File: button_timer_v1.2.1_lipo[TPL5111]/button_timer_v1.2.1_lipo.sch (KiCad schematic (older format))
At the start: 23 parts, among them J1 Conn_01x05_Female, SW1 SW_Push, SW2 SW_Push, U2 AP2112K-3.3, U3 TPL5111, X1 ESP-12E

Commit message: 3D Models etwas verbessert
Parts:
- C5: footprint handsolder:C_0805_2012handsodermod -> handsolder:C_0402_1005Metric_Pad0.74x0.62mm_HandSoldermod
- J1: footprint Connector_PinHeader_2.54mm:PinHeader_1x05_P2.54mm_Vertical -> Connector_PinSocket_2.54mm:PinSocket_1x05_P2.54mm_Vertical
- SW1: footprint Button_Switch_THT:SW_PUSH_6mm -> Button_Switch_THT:SW_PUSH_6mm_H8mm
- SW2: footprint Button_Switch_SMD:SW_SPST_EVQPE1 -> Button_Switch_SMD:SW_SPST_B3U-1000P
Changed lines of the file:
@@
 F 0 "SW2" H 8000 3385 50  0000 C CNN
 F 1 "SW_Push" H 8000 3294 50  0000 C CNN
-F 2 "Button_Switch_SMD:SW_SPST_EVQPE1" H 8000 3300 50  0001 C CNN
+F 2 "Button_Switch_SMD:SW_SPST_B3U-1000P" H 8000 3300 50  0001 C CNN
 F 3 "~" H 8000 3300 50  0001 C CNN
 	1    8000 3100
@@
 F 0 "SW1" H 1100 5935 50  0000 C CNN
 F 1 "SW_Push" H 1100 5844 50  0000 C CNN
-F 2 "Button_Switch_THT:SW_PUSH_6mm" H 1100 5850 50  0001 C CNN
+F 2 "Button_Switch_THT:SW_PUSH_6mm_H8mm" H 1100 5850 50  0001 C CNN
 F 3 "~" H 1100 5850 50  0001 C CNN
 	1    1100 5650
@@
 F 0 "J1" H 8128 3476 50  0000 L CNN
 F 1 "Conn_01x05_Female" H 8128 3385 50  0000 L CNN
-F 2 "Connector_PinHeader_2.54mm:PinHeader_1x05_P2.54mm_Vertical" H 8100 3450 50  0001 C CNN
+F 2 "Connector_PinSocket_2.54mm:PinSocket_1x05_P2.54mm_Vertical" H 8100 3450 50  0001 C CNN
 F 3 "~" H 8100 3450 50  0001 C CNN
 	1    8100 3450
@@
 F 0 "C5" V 2148 4850 50  0000 C CNN
 F 1 "100nF" V 2239 4850 50  0000 C CNN
-F 2 "handsolder:C_0805_2012handsodermod" H 2438 4700 50  0001 C CNN
+F 2 "handsolder:C_0402_1005Metric_Pad0.74x0.62mm_HandSoldermod" H 2438 4700 50  0001 C CNN
 F 3 "~" H 2400 4850 50  0001 C CNN
 	1    2400 4850

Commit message: cap between esp vcc and ground added
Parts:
- added C6: TAJB476M010TNJ, CAPPM3528X210N, symbol SamacSys_Parts:TAJB476M010TNJ
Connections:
- net GND: now also C6.2
- net VCC: now also C6.1
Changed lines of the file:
@@
 Text Label 2250 4850 2    50   ~ 0
 GND
+Text Label 5300 4200 0    50   ~ 0
+GND
+$Comp
+L SamacSys_Parts:TAJB476M010TNJ C6
+U 1 1 603708C9
+P 5300 3700
+F 0 "C6" V 5504 3830 50  0000 L CNN
+F 1 "TAJB476M010TNJ" V 5595 3830 50  0000 L CNN
+F 2 "CAPPM3528X210N" H 5650 3750 50  0001 L CNN
+F 3 "http://datasheets.avx.com/TAJ.pdf" H 5650 3650 50  0001 L CNN
+F 4 "Tantalum Capacitors - Solid SMD 10volts 47uF 20%" H 5650 3550 50  0001 L CNN "Description"
+F 5 "2.1" H 5650 3450 50  0001 L CNN "Height"
+F 6 "AVX" H 5650 3350 50  0001 L CNN "Manufacturer_Name"
+F 7 "TAJB476M010TNJ" H 5650 3250 50  0001 L CNN "Manufacturer_Part_Number"
+F 8 "581-TAJB476M010TNJ" H 5650 3150 50  0001 L CNN "Mouser Part Number"
+F 9 "https://www.mouser.co.uk/ProductDetail/AVX/TAJB476M010TNJ?qs=pYVYkI7xuRVorIKKgcxm0A%3D%3D" H 5650 3050 50  0001 L CNN "Mouser Price/Stock"
+F 10 "TAJB476M010TNJ" H 5650 2950 50  0001 L CNN "Arrow Part Number"
+F 11 "https://www.arrow.com/en/products/tajb476m010tnj/avx" H 5650 2850 50  0001 L CNN "Arrow Price/Stock"
+	1    5300 3700
+	0    1    1    0
+$EndComp
 $EndSCHEMATC

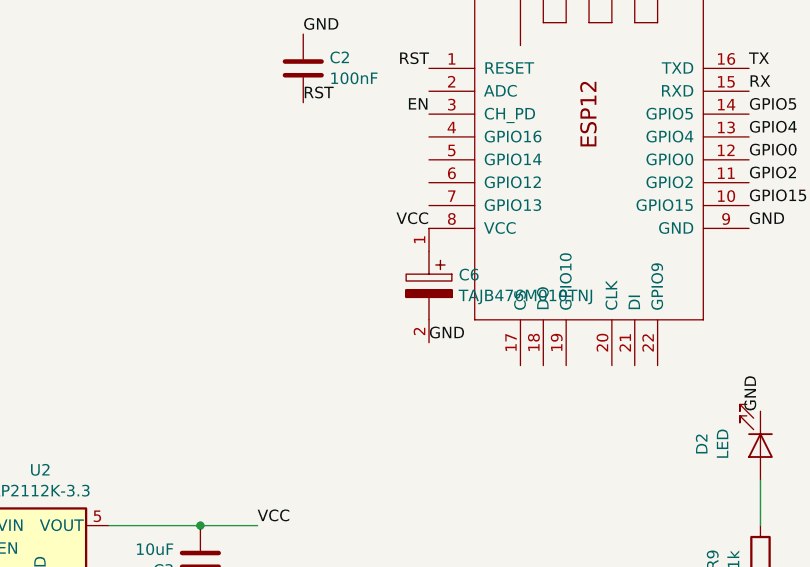
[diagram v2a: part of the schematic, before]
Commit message: Added 100nF decoupling capacitors between VCC and Ground of the ESP
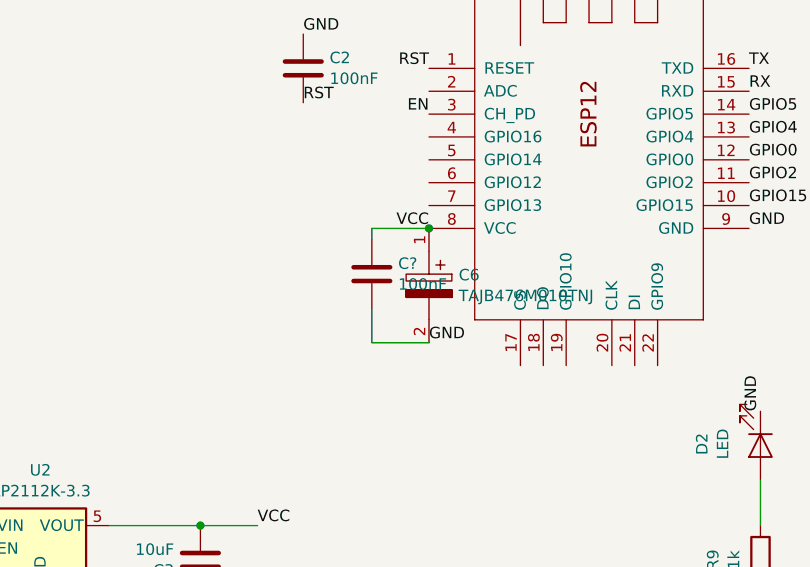
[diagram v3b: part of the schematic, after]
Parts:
- added C?: 100nF, handsolder:C_0402_1005Metric_Pad0.74x0.62mm_HandSoldermod, symbol Device:C
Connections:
- net GND: now also C?.2
- net VCC: now also C?.1
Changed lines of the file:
@@
 	0    1    1    0
 $EndComp
+$Comp
+L Device:C C?
+U 1 1 60367C97
+P 5050 3900
+F 0 "C?" H 5165 3946 50  0000 L CNN
+F 1 "100nF" H 5165 3855 50  0000 L CNN
+F 2 "handsolder:C_0402_1005Metric_Pad0.74x0.62mm_HandSoldermod" H 5088 3750 50  0001 C CNN
+F 3 "~" H 5050 3900 50  0001 C CNN
+	1    5050 3900
+	1    0    0    -1
+$EndComp
+Wire Wire Line
+	5050 3750 5050 3700
+Wire Wire Line
+	5050 3700 5300 3700
+Connection ~ 5300 3700
+Wire Wire Line
+	5050 4050 5050 4200
+Wire Wire Line
+	5050 4200 5300 4200
 $EndSCHEMATC
